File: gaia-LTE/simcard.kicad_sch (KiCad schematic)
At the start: 2 parts, among them J4 SIM8051-6-0-14-00-A_REVD6

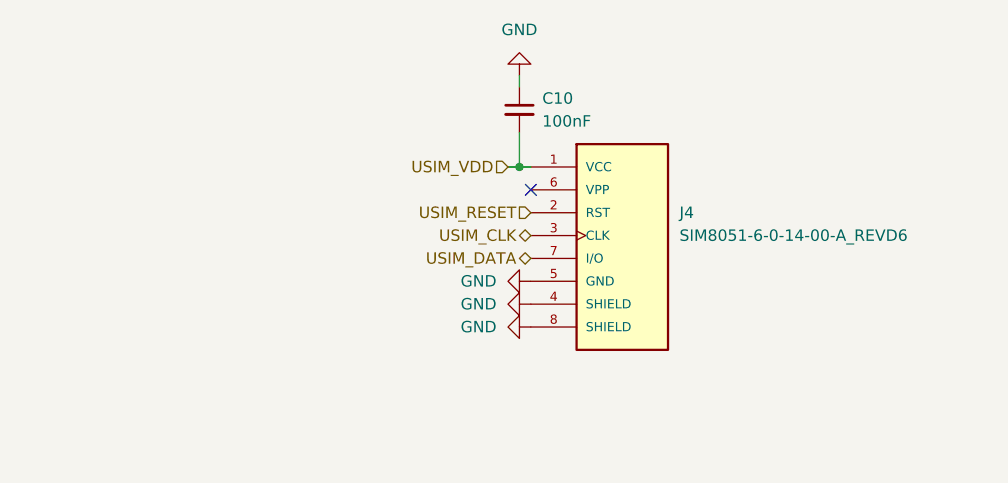
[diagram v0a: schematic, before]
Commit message: adding TVS diodes 1/2
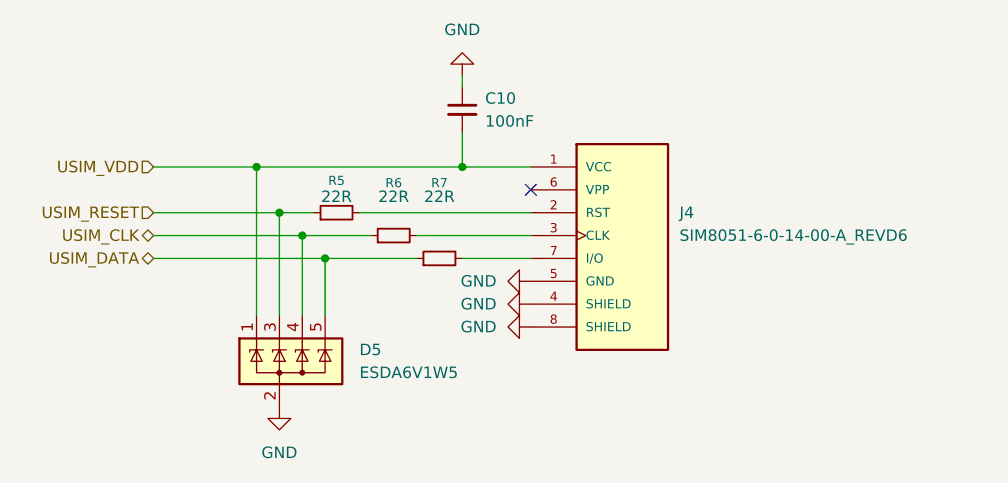
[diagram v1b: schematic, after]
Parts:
- added D5: ESDA6V1W5, Package_TO_SOT_SMD:SOT-23-5, symbol Power_Protection:ESDA6V1SC5
- added R5, R6, R7: 22R, symbol Device:R_Small
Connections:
- net GND: now also D5.2 (A)
- net USIM_CLK: now also D5.4 (K), R6.1; no longer J4.3 (CLK)
- net USIM_DATA: now also D5.5 (K), R7.1; no longer J4.7 (I/O)
- net USIM_RESET: now also D5.3 (K), R5.1; no longer J4.2 (RST)
- net USIM_VDD: now also D5.1 (K)
- new net: J4.2 (RST), R5.2
- new net: J4.3 (CLK), R6.2
- new net: J4.7 (I/O), R7.2
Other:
- moved on the sheet: C10
